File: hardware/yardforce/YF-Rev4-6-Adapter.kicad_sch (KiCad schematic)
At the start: 32 parts, among them J1 USB_OTG, J2 JTAG ARM-10, J3 YF-Rev6-B, J4 YF-Rev6-A, J5 YF-Rev4-A, J6 YF-Rev4-B, J7 OM UI Board, U1 XC6220B331MR, U2 ESP32-S3-WROOM-1, U3 TCA9555PWR

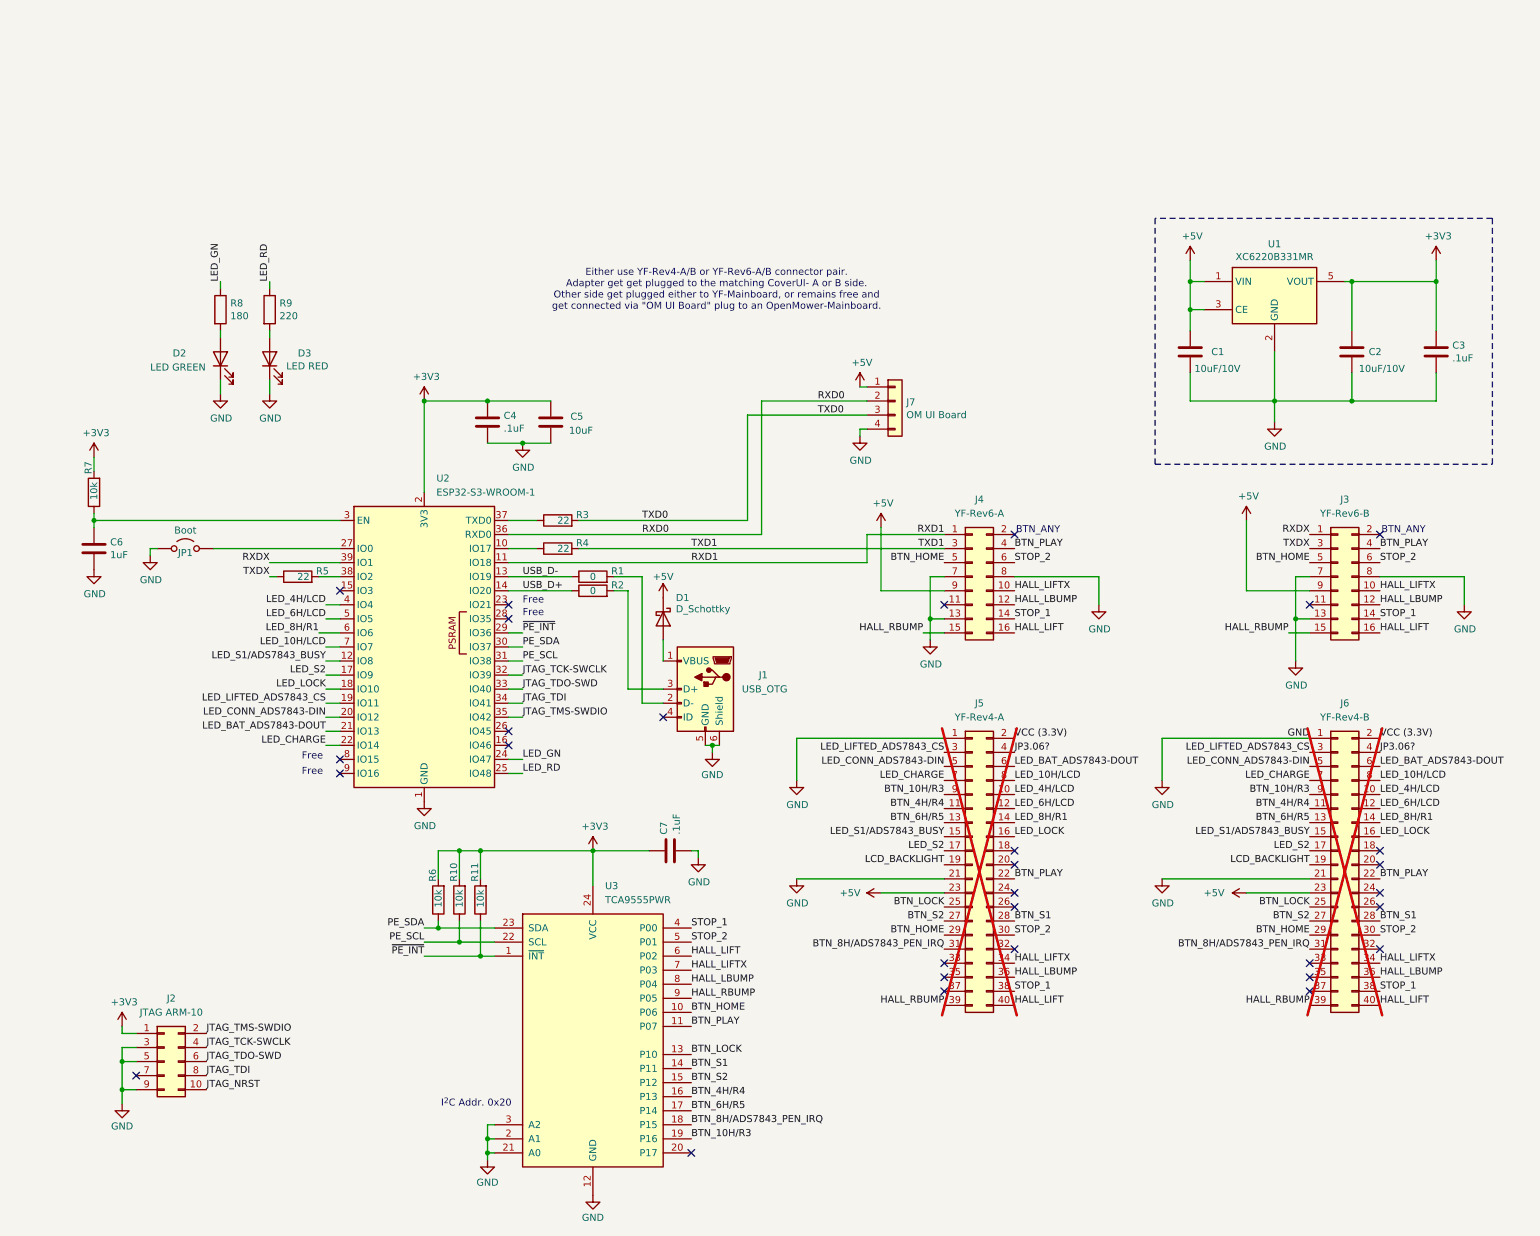
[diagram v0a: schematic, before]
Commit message: Fix ERC issues
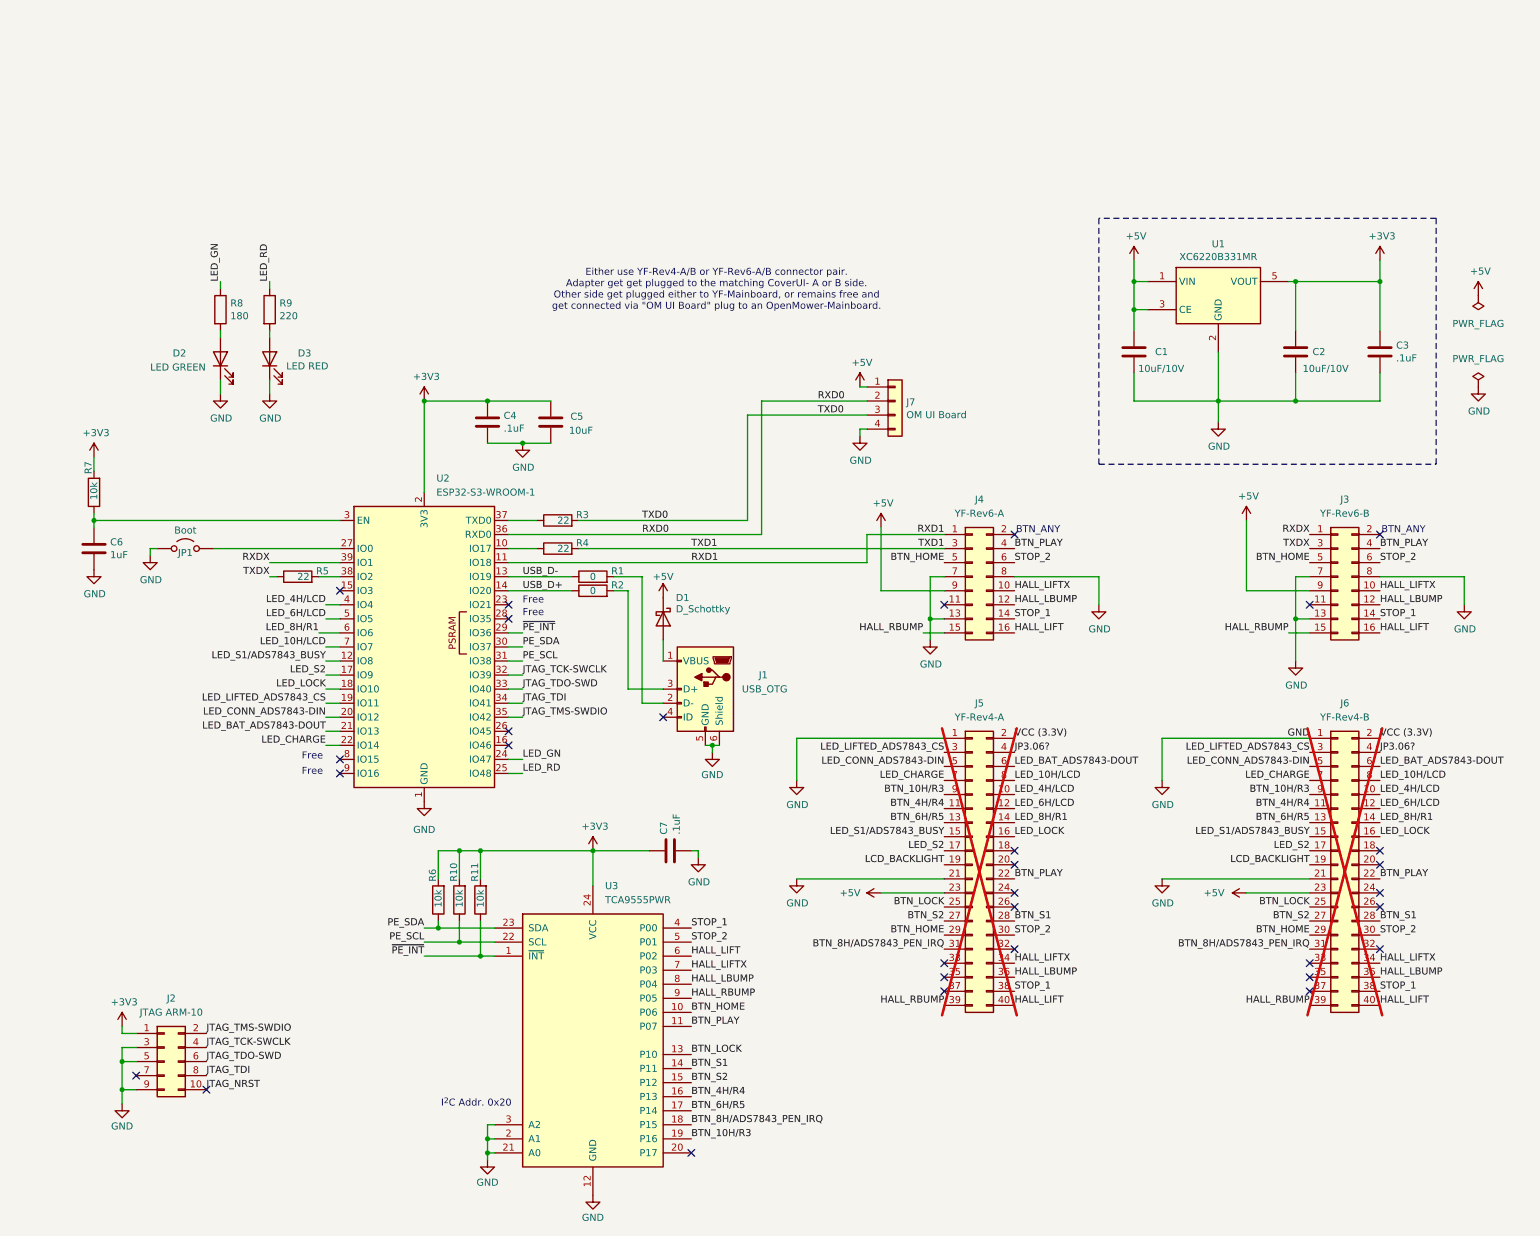
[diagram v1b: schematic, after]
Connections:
- no-connect marks 30 -> 31
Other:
- moved on the sheet: C1, C2, C3, U1

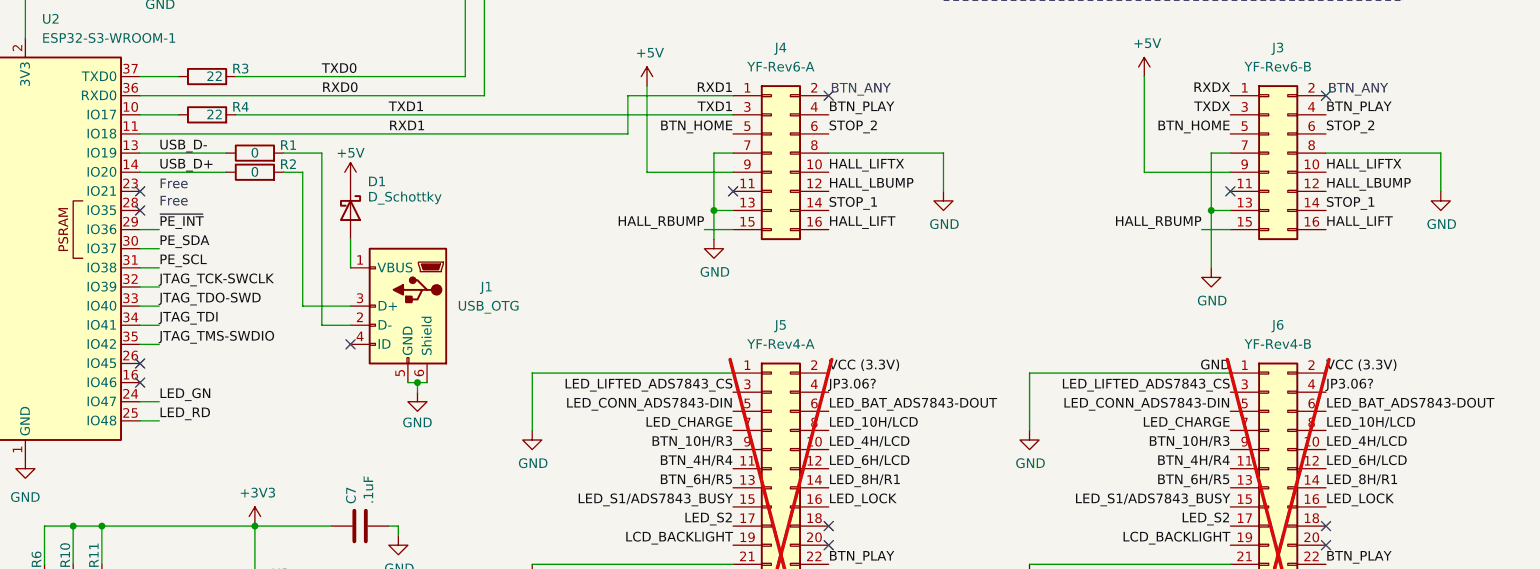
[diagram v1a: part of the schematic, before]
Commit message: Add Rev4 3V3 solder jumper
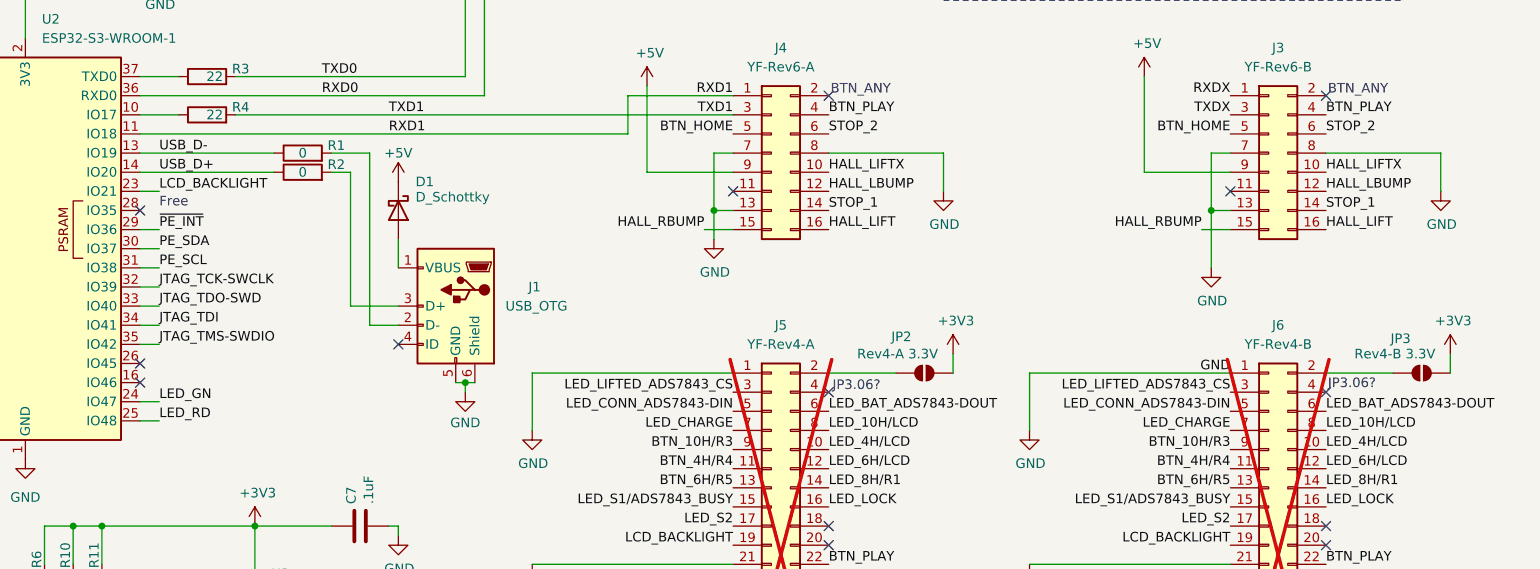
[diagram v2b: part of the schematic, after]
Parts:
- added JP2: Rev4-A 3.3V, Jumper:SolderJumper-2_P1.3mm_Open_RoundedPad1.0x1.5mm, symbol Jumper:SolderJumper_2_Open
- added JP3: Rev4-B 3.3V, Jumper:SolderJumper-2_P1.3mm_Open_RoundedPad1.0x1.5mm, symbol Jumper:SolderJumper_2_Open
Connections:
- net +3V3: now also JP2.2 (B), JP3.2 (B)
- net LCD_BACKLIGHT: now also U2.23 (IO21)
- net JP3.06?: no longer names the net of J6.4 (Pin_4)
- net JP3.06?: no longer J5.4 (Pin_4)
- net VCC (3.3V): no longer names the net of J6.2 (Pin_2)
- net VCC (3.3V): now also JP3.1 (A); no longer J5.2 (Pin_2)
- new net: J5.2 (Pin_2), JP2.1 (A)
- no-connect marks 31 -> 32
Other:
- note added: "JP3.06?"
- moved on the sheet: D1, J1, R1, R2

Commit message: BOM Update
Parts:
- C1, C2: value 10uF/10V -> 10uF
- D1: JLCPCB (none) -> C82288
- J1: JLCPCB C5454937 -> C668588; MF XUNPU -> SHOU HAN; MFR TYPEC-300-BCP16H65 -> MICRO 180°ZB
- JP1: JLCPCB (none) -> C5360898; MF (none) -> ZHOURI; MF Part (none) -> PZ2.54-1*2
- U2: JLCPCB (none) -> C2913197; MF (none) -> Espressif Systems; MF Part (none) -> ESP32-S3-WROOM-1-N4
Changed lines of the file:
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@@
 			)
 		)
+		(property "MF" "ZHOURI"
+			(at 44.45 74.93 0)
+			(effects
+				(font
+					(size 1.27 1.27)
+				)
+				(hide yes)
+			)
+		)
+		(property "MF Part" "PZ2.54-1*2"
+			(at 44.45 74.93 0)
+			(effects
+				(font
+					(size 1.27 1.27)
+				)
+				(hide yes)
+			)
+		)
+		(property "JLCPCB" "C5360898"
+			(at 44.45 74.93 0)
+			(effects
+				(font
+					(size 1.27 1.27)
+				)
+				(hide yes)
+			)
+		)
 		(pin "2"
 		)
@@
 			)
 		)
+		(property "JLCPCB" "C82288"
+			(at 137.16 87.63 90)
+			(effects
+				(font
+					(size 1.27 1.27)
+				)
+				(hide yes)
+			)
+		)
 		(pin "1"
 		)
@@
 			)
 		)
-		(property "Value" "10uF/10V"
+		(property "Value" "10uF"
 			(at 246.38 42.418 0)
 			(effects
@@
 			)
 		)
-		(property "Description" "USB mini/micro connector"
+		(property "Description" "1A USB 2.0 Direct Insert 5P Female, Micro-B Plugin USB"
 			(at 144.78 100.33 0)
 			(effects
@@
 			)
 		)
-		(property "MFR" "TYPEC-300-BCP16H65"
+		(property "MFR" "MICRO 180°ZB"
 			(at 144.78 100.33 0)
 			(effects
@@
 			)
 		)
-		(property "JLCPCB" "C5454937"
+		(property "JLCPCB" "C668588"
 			(at 144.78 100.33 0)
 			(effects
@@
 			)
 		)
-		(property "MF" "XUNPU"
+		(property "MF" "SHOU HAN"
 			(at 144.78 100.33 0)
 			(effects
@@
 			)
 		)
+		(property "MF" "Espressif Systems"
+			(at 87.63 92.71 0)
+			(effects
+				(font
+					(size 1.27 1.27)
+				)
+				(hide yes)
+			)
+		)
+		(property "MF Part" "ESP32-S3-WROOM-1-N4"
+			(at 87.63 92.71 0)
+			(effects
+				(font
+					(size 1.27 1.27)
+				)
+				(hide yes)
+			)
+		)
+		(property "JLCPCB" "C2913197"
+			(at 87.63 92.71 0)
+			(effects
+				(font
+					(size 1.27 1.27)
+				)
+				(hide yes)
+			)
+		)
 		(pin "40"
 		)
@@
 			)
 		)
-		(property "Value" "10uF/10V"
+		(property "Value" "10uF"
 			(at 216.662 42.418 0)
 			(effects

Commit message: Add HW Prototype v0.1
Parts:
- removed C5: 10uF, Capacitor_SMD:C_0603_1608Metric, symbol Device:C
- removed J2: JTAG ARM-10, Connector_IDC:IDC-Header_2x05_P2.54mm_Vertical, symbol Connector_Generic:Conn_02x05_Odd_Even
- removed JP1: Boot, Connector_PinSocket_2.54mm:PinSocket_1x02_P2.54mm_Vertical, symbol Jumper:Jumper_2_Open
- removed U2: ESP32-S3-WROOM-1, libs:ESP32-S3-WROOM-1_MOD, symbol RF_Module:ESP32-S3-WROOM-1
- added ANT1: 2.4Ghz, libs:PCB_Antenna_2.4GHz_Left, symbol PCB_Antenna:PCB_Trace24
- added C10, C11: 10pF, Capacitor_SMD:C_0402_1005Metric, symbol Device:C
- added C12, C15, C16, C17, C18: .1uF, Capacitor_SMD:C_0402_1005Metric, symbol Device:C
- added C14: 1uF, Capacitor_SMD:C_0402_1005Metric, symbol Device:C
- added C8: DNP, Capacitor_SMD:C_0402_1005Metric, symbol Device:C
- added C9: 0.8pF, Capacitor_SMD:C_0402_1005Metric, symbol Device:C
- added D4: PDZ3.3B,115, Diode_SMD:D_SOD-323, symbol Device:D_Zener
- added GPIO33, GPIO47, GPIO48: TestPoint, TestPoint:TestPoint_Pad_1.0x1.0mm, symbol Connector:TestPoint
- added J2: TC2050-IDC, libs:TAG-CONNECT_TC2050-IDC, symbol TC2050-IDC:TC2050-IDC
- added J8: Shell Stop, Connector_JST:JST_XH_B3B-XH-A_1x03_P2.50mm_Vertical, symbol Connector_Generic:Conn_01x03
- added J9: Rain, Connector_JST:JST_XH_B2B-XH-A_1x02_P2.50mm_Vertical, symbol Connector_Generic:Conn_01x02
- added L1: 3.9nH, Inductor_SMD:L_0402_1005Metric, symbol Device:FerriteBead
- added L2: 2.0nH, Inductor_SMD:L_0402_1005Metric, symbol Device:FerriteBead
- added L3: 24nH, Inductor_SMD:L_0402_1005Metric, symbol Device:FerriteBead
- added R12: 10k, Resistor_SMD:R_0603_1608Metric, symbol Device:R
- added S1: RST, libs:SW_TS-1187A-B-A-B, symbol TS-1187A-B-A-B:TS-1187A-B-A-B
- added U4: ESP32-S3-FH4R2, Package_DFN_QFN:QFN-56-1EP_7x7mm_P0.4mm_EP4x4mm_ThermalVias, symbol PCM_Espressif:ESP32-S3
- added Y1: 40MHz 10.5pF ±10ppm, Crystal:Crystal_SMD_2016-4Pin_2.0x1.6mm, symbol Crystal_SMD:XRCGB40M000F4M02R0
- C1, C2: JLCPCB C76608 -> (none); LCSC (none) -> C19702
- C3, C7: JLCPCB C41851 -> (none); LCSC (none) -> C1525
- C4: JLC (none) -> C307331; JLCPCB C41851 -> (none); LCSC (none) -> C1525; Stock_PN C-402-.1uF-16V-X7R -> (none)
- C6: JLCPCB C76999 -> (none); LCSC (none) -> C52923
- D1: JLCPCB C82288 -> (none); LCSC (none) -> C82288
- D2: JLCPCB KT-0603G -> (none); LCSC (none) -> C12624
- D3: JLCPCB KT-0603R -> (none); LCSC (none) -> C2286
- J1: JLCPCB C668588 -> (none); LCSC (none) -> C668588
- J3: JLCPCB C3320355 / C601981 -> (none); LCSC (none) -> C3320355 / C601981
- J4: JLCPCB C3320355 -> (none); LCSC (none) -> C3320355
- J5: JLCPCB C5909928 / C3029524 -> (none); LCSC (none) -> C5909928 / C3029524; now fitted
- J6: JLCPCB C5909928 -> (none); LCSC (none) -> C5909928; now fitted
- R1, R2: footprint Resistor_SMD:R_0603_1608Metric -> Resistor_SMD:R_0402_1005Metric; JLCPCB C21189 -> (none); LCSC (none) -> C17168
- R10, R11, R6, R7: JLCPCB C15401 -> (none); LCSC (none) -> C25804
- R3, R4, R5: JLCPCB C23345 -> (none); LCSC (none) -> C23345
- R8: value 180 -> 200; LCSC (none) -> C8218; Part Number RC0603FR-07180RL -> (none); Stock_PN R-603-180-.1W-1% -> (none)
- R9: Digikey 311-220HRCT-ND -> (none); LCSC (none) -> C22962; Part Number RC0603FR-07220RL -> (none); Stock_PN R-603-220-.1W-1% -> (none)
- U1: value XC6220B331MR -> AMS1117-3.3; footprint Package_TO_SOT_SMD:SOT-23-5 -> Package_TO_SOT_SMD:SOT-223-3_TabPin2; symbol Regulator_Linear:XC6220B331MR -> Regulator_Linear:AMS1117-3.3; Digikey 893-1133-1-ND -> (none); LCSC C86534 -> C6186; Part Number XC6220B331MR -> (none); Stock_PN U-XC6220B331MR -> (none)
- U3: LCSC (none) -> C465732
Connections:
- net +3V3: now also U1.2 (VO), C14.1, C15.1, C16.1, C17.1, C18.1, J2.1, L2.2, U4.20 (VDD3P3_RTC), U4.29 (VDD_SPI), U4.46 (VDD3P3_CPU), U4.55 (VDDA), U4.56 (VDDA); no longer C4.1, U1.5 (VOUT)
- net +5V: no longer U1.1 (VIN)
- net BTN_PLAY: now also U4.5 (GPIO0/BOOT); no longer U3.11 (P07)
- net GND: now also U1.1 (GND), ANT1.2, C10.2, C11.2, C12.1, C14.2, C15.2, C16.2, C17.2, C18.2, C8.2, C9.2, D4.2 (A), J2.3, J2.5, J2.9, J8.2 (Pin_2), J9.2 (Pin_2), S1.A, S1.B, U4.57 (GND), Y1.2, Y1.4; no longer U1.2 (GND)
- net JTAG_TCK-SWCLK: now also J2.4, U4.44 (MTCK/JTAG/GPIO39)
- net JTAG_TDI: now also J2.8, U4.47 (MTDI/JTAG/GPIO41)
- net JTAG_TDO-SWD: now also J2.6, U4.45 (MTDO/JTAG/GPIO40)
- net JTAG_TMS-SWDIO: now also J2.2, U4.48 (MTMS/JTAG/GPIO42)
- net LCD_BACKLIGHT: now also U4.33 (SPICLK/GPIO30)
- net LED_10H/LCD: now also U4.18 (GPIO13/ADC2_CH2)
- net LED_4H/LCD: now also U4.15 (GPIO10/ADC1_CH9)
- net LED_6H/LCD: now also U4.16 (GPIO11/ADC2_CH0)
- net LED_8H/R1: now also U4.17 (GPIO12/ADC2_CH1)
- net LED_BAT_ADS7843-DOUT: now also U4.8 (GPIO3/ADC1_CH2)
- net LED_CHARGE: now also U4.9 (GPIO4/ADC1_CH3)
- net LED_CONN_ADS7843-DIN: now also U4.7 (GPIO2/ADC1_CH1)
- net LED_GN: now also U4.34 (SPIQ/GPIO31)
- net LED_LIFTED_ADS7843_CS: now also U4.6 (GPIO1/ADC1_CH0)
- net LED_LOCK: now also U4.32 (SPICS0/GPIO29)
- net LED_RD: now also U4.35 (SPID/GPIO32)
- net LED_S1/ADS7843_BUSY: now also U4.30 (SPIHD/GPIO27)
- net LED_S2: now also U4.31 (SPIWP/GPIO28)
- net PE_SCL: now also U4.41 (GPIO36)
- net PE_SDA: now also U4.40 (GPIO35)
- net RXD0: now also U4.50 (U0RXD/PROG/GPIO44)
- net RXD1: now also U4.24 (GPIO18/ADC2_CH7)
- net RXDX: now also U4.43 (GPIO38)
- net USB_D+: now also J1.3 (D+), R2.2; no longer R2.1
- net USB_D-: now also J1.2 (D-), R1.2; no longer R1.1
- net ~{PE_INT}: now also U4.39 (GPIO34)
- net at R5.2: now also U4.42 (GPIO37)
- net at C6.1, R7.1: now also S1.C, S1.D, U4.4 (CHIP_PU/RESET)
- net at R4.1: now also U4.23 (GPIO17/ADC2_CH6)
- net Shell Stop 2: now reaches U3.20 (P17)
- net Shell Stop 2: now also J8.3 (Pin_3)
- net at R3.1: now also U4.49 (U0TXD/PROG/GPIO43)
- new net: R2.1, U4.26 (GPIO20/USB_D+/ADC2_CH9)
- new net: C11.1, L3.1, Y1.1
- new net: C10.1, U4.53 (XTAL_N), Y1.3
- new net: C4.1, D4.1 (K), J9.1 (Pin_1), R12.2
- new net: ANT1.1, C8.1, L1.1
- new net: C9.1, L1.2, U4.1 (LNA_IN/RF)
- new net: R1.1, U4.25 (GPIO19/USB_D-/ADC2_CH8)
- new net: GPIO48.1, U4.36 (SPICLK_N/GPIO48)
- new net: GPIO47.1, U4.37 (SPICLK_P/GPIO47)
- new net: GPIO33.1, U4.38 (GPIO33)
- new net: L3.2, U4.54 (XTAL_P)
- new net RAIN: R12.1, U4.22 (GPIO16/ADC2_CH5/XTAL_32K_N)
- new net Shell Stop 1: J8.1 (Pin_1), U3.11 (P07)
- new net VDD3P3: C12.2, L2.1, U4.2 (VDD3P3), U4.3 (VDD3P3)
- no-connect marks 32 -> 36
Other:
- note added: "If used should become a LED"
- note added: "JTAG-ARM10"
- note added: "VDD_SPI Voltage Control"
- note removed: "Free"
- moved on the sheet: C1, C2, C3, C6, C7, D1, D2, D3, J1, J3, J4, J7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

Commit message: Change Micro-USB part to U255-051N-4BH70-SS
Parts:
- J1: footprint libs:USB_Micro-B_Wuerth_614105150721_Vertical -> libs:MINI-USB-SMD_U255-051N-4BH70-XS; LCSC C668588 -> C437033; MF SHOU HAN -> XKB Connection; MFR MICRO 180°ZB -> U255-051N-4BH70-SS
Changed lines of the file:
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@@
 			)
 		)
-		(property "Footprint" "libs:USB_Micro-B_Wuerth_614105150721_Vertical"
+		(property "Footprint" "libs:MINI-USB-SMD_U255-051N-4BH70-XS"
 			(at 29.21 73.66 0)
 			(effects
@@
 			)
 		)
-		(property "Description" "1A USB 2.0 Direct Insert 5P Female, Micro-B Plugin USB"
+		(property "Description" "USB 2.0 1.8A 1 235℃ Direct Insert 5P Female -40℃~+85℃ Gold Brass Alloy Micro-B Plugin USB Connectors"
 			(at 33.02 72.39 0)
 			(effects
@@
 			)
 		)
-		(property "MFR" "MICRO 180°ZB"
+		(property "MFR" "U255-051N-4BH70-SS"
 			(at 33.02 72.39 0)
 			(effects
@@
 			)
 		)
-		(property "JLCPCB" ""
-			(at 33.02 72.39 0)
-			(effects
-				(font
-					(size 1.27 1.27)
-				)
-				(hide yes)
-			)
-		)
-		(property "MF" "SHOU HAN"
+		(property "MF" "XKB Connection"
 			(at 33.02 72.39 0)
 			(effects
@@
 			)
 		)
-		(property "LCSC" "C668588"
+		(property "LCSC" "C437033"
 			(at 33.02 72.39 0)
 			(effects
